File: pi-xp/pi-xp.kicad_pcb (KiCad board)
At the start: 2 copper layers, 30.5 x 65.4 mm, 25 parts

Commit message: pi_xp v1.1
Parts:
- F1: footprint Fuse_Holders_and_Fuses:BladeFuse-Mini_Keystone_3568 -> Fuse_Holders_and_Fuses:Fuse_TE5_Littlefuse-395Series
- OUT1, OUT2, OUT3: value CONN_01X03 -> CONN_01X02; footprint Pin_Headers:Pin_Header_Straight_1x03_Pitch2.54mm -> Pin_Headers:Pin_Header_Straight_1x02_Pitch2.54mm
- moved 5VIN1 52.2 mm to (94.6, 80.6), turned to 270 degrees
- moved F1 22.7 mm to (104.1, 132.1), turned to 180 degrees
- moved 12VOUT1 17.1 mm to (92.7, 109.2)
- moved 12VOUT2 16.5 mm to (92.7, 97.8)
- moved FAN1 16.2 mm to (92.7, 85.1), turned to 0 degrees
- moved OUT1 3.81 mm to (101.0, 125.7), turned to 180 degrees
- moved OUT2 3.81 mm to (104.8, 125.7), turned to 180 degrees
- moved OUT3 3.81 mm to (108.6, 125.7), turned to 180 degrees
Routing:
- net V12: track 0.00 -> 20.4 mm
- net PWM: track 31.1 -> 24.7 mm
- net OUTPUT1: track 17.7 -> 16.4 mm
- net OUTPUT2: track 12.8 -> 11.5 mm
- net GND: track 8.25 -> 7.62 mm
- net OUTPUT3: track 7.18 -> 6.66 mm
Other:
- board text added: "OyaMist PI_XP1.1"
- board text removed: "OyaMist PI_XP1.0"

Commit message: PI_XP1.2
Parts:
- OUT1, OUT2, OUT3: value CONN_01X02 -> CONN_01X03; footprint Pin_Headers:Pin_Header_Straight_1x02_Pitch2.54mm -> Pin_Headers:Pin_Header_Straight_1x03_Pitch2.54mm
- moved 12VIN1 1.27 mm to (92.7, 119.4)
- moved 12VOUT2 1.27 mm to (92.7, 99.1)
- moved OUT1 1.27 mm to (101.0, 127.0)
- moved OUT2 1.27 mm to (104.8, 127.0)
- moved OUT3 1.27 mm to (108.6, 127.0)
- moved FAN1 0.63 mm to (92.7, 85.7)
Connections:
- OUT1 pad 2: OUTPUT1 -> PI3V3
- OUT2 pad 2: OUTPUT2 -> PI3V3
- OUT3 pad 2: OUTPUT3 -> PI3V3
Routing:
- net OUTPUT1: track 16.4 -> 15.9 mm
- net OUTPUT2: track 11.5 -> 11.0 mm
- net OUTPUT3: track 6.66 -> 6.13 mm
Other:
- board text added: "OyaMist PI_XP1.2"
- board text removed: "OyaMist PI_XP1.1"

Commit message: v1.3
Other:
- board text added: "12V"
- board text added: "2"
- board text added: "3"
- board text added: "3V3"
- board text added: "IN"
- board text added: "OUT"
- board text added: "OyaMist PI_XP1.3"
- board text added: "PWM"
- board text added: "SCL"
- board text added: "SDA"
- board text added: "W1"
- board text added: "W1/1"
- board text removed: "1WIRE1"
- board text removed: "BLINK1"
- board text removed: "CLK"
- board text removed: "OyaMist PI_XP1.2"

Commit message: v1.3
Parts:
- moved BLINK1 1.77 mm to (109.2, 72.6)
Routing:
- net PI3V3_LED: track 5.23 -> 6.30 mm
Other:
- board text added: "39"
- board text added: "FUSE 5A/12V"
- board text added: "LED"
- board text added: "OyaMist Backplane"
- board text added: "PI-XP v1.3"
- board text removed: "FUSE 5A"
- board text removed: "OyaMist PI_XP1.3"

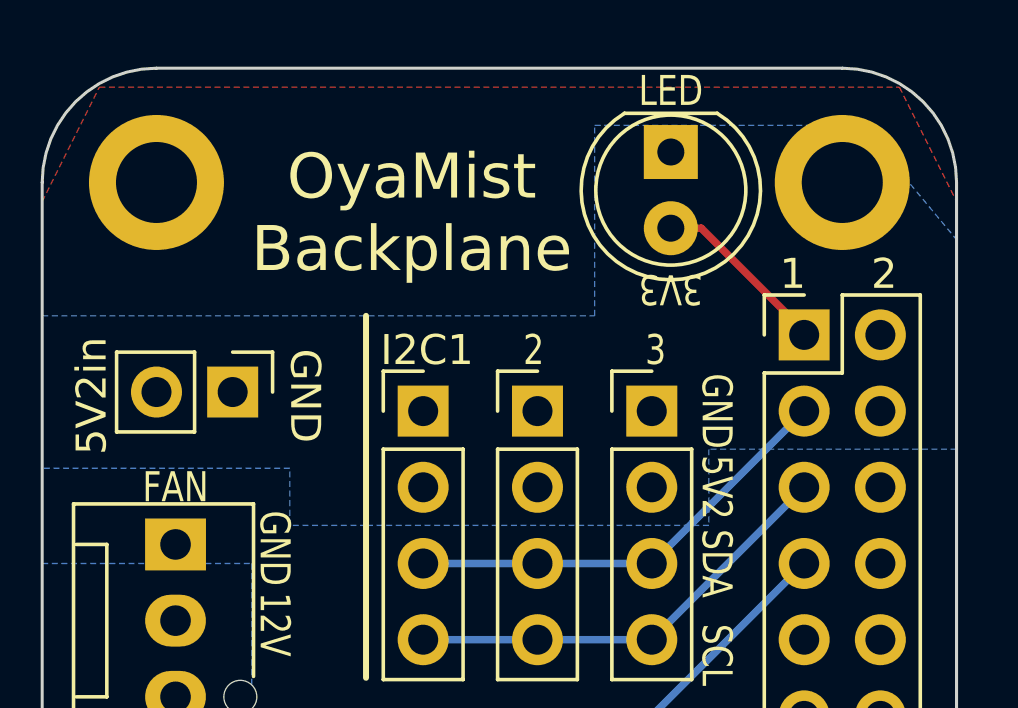
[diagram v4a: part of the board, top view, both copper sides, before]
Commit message: v1.4 I2C 3v3
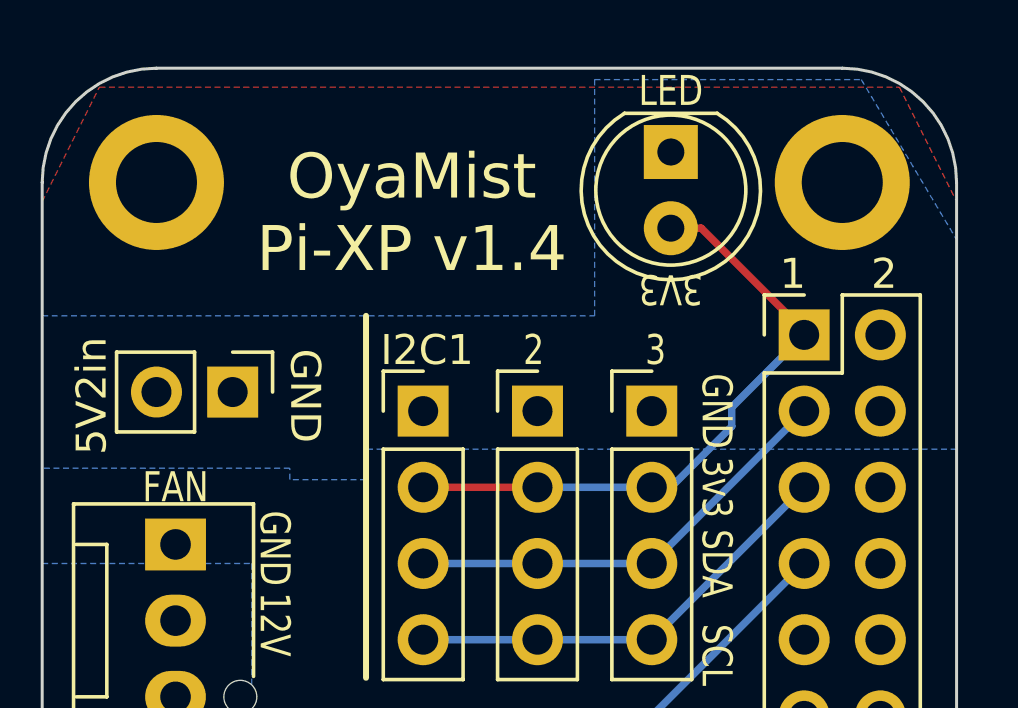
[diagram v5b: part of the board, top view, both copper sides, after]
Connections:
- I2C1 pad 2: 5V2 -> PI3V3_LED
- I2C2 pad 2: 5V2 -> PI3V3_LED
- I2C3 pad 2: 5V2 -> PI3V3_LED
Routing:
- net PI3V3_LED: track 6.30 -> 21.3 mm
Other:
- board text added: "Backplane"
- board text added: "OyaMist Pi-XP v1.4"
- board text removed: "5V2"
- board text removed: "OyaMist Backplane"
- board text removed: "PI-XP v1.3"
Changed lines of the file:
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@@
     (links 61)
     (no_connects 0)
-    (area 75.184 64.008 135.636 141.732)
+    (area 75.642857 64.135 135.635 141.765001)
     (thickness 1.6)
     (drawings 115)
-    (tracks 61)
+    (tracks 66)
     (zones 0)
     (modules 25)
@@
       (net 28 GND) (clearance -0.5))
     (pad 2 thru_hole oval (at 0 2.54) (size 1.7 1.7) (drill 1) (layers *.Cu *.Mask)
-      (net 30 5V2) (clearance -0.5))
+      (net 36 PI3V3_LED) (clearance -0.5))
     (pad 3 thru_hole oval (at 0 5.08) (size 1.7 1.7) (drill 1) (layers *.Cu *.Mask)
       (net 1 I2C_DAT))
@@
       (net 28 GND) (clearance -0.5))
     (pad 2 thru_hole oval (at 0 2.54) (size 1.7 1.7) (drill 1) (layers *.Cu *.Mask)
-      (net 30 5V2) (clearance -0.5))
+      (net 36 PI3V3_LED) (clearance -0.5))
     (pad 3 thru_hole oval (at 0 5.08) (size 1.7 1.7) (drill 1) (layers *.Cu *.Mask)
       (net 1 I2C_DAT))
@@
       (net 28 GND))
     (pad 2 thru_hole oval (at 0 2.54) (size 1.7 1.7) (drill 1) (layers *.Cu *.Mask)
-      (net 30 5V2) (clearance -1))
+      (net 36 PI3V3_LED) (clearance -1))
     (pad 3 thru_hole oval (at 0 5.08) (size 1.7 1.7) (drill 1) (layers *.Cu *.Mask)
       (net 1 I2C_DAT))
@@
     (effects (font (size 1 0.8) (thickness 0.15)) (justify mirror))
   )
-  (gr_text "PI-XP\nv1.3" (at 100.076 74.676) (layer B.SilkS)
+  (gr_text Backplane (at 100.838 71.882) (layer B.SilkS)
     (effects (font (size 1.5 1.5) (thickness 0.3)) (justify mirror))
   )
@@
     (effects (font (size 1 0.8) (thickness 0.15)) (justify mirror))
   )
-  (gr_text 5V2 (at 110.744 83.82 270) (layer B.SilkS)
+  (gr_text "3v3\n" (at 110.744 83.82 270) (layer B.SilkS)
     (effects (font (size 1 0.8) (thickness 0.15)) (justify mirror))
   )
@@
     (effects (font (size 1 0.8) (thickness 0.15)))
   )
-  (gr_text 5V2 (at 110.744 83.82 270) (layer F.SilkS)
+  (gr_text "3v3\n" (at 110.744 83.82 270) (layer F.SilkS)
     (effects (font (size 1 0.8) (thickness 0.15)))
   )
@@
     (effects (font (size 1 0.8) (thickness 0.15)))
   )
-  (gr_text "OyaMist\nBackplane\n" (at 100.584 74.676) (layer F.SilkS)
+  (gr_text "OyaMist\nPi-XP v1.4\n" (at 100.584 74.676) (layer F.SilkS)
     (effects (font (size 1.5 1.5) (thickness 0.3)))
   )
@@
   (segment (start 108.585 114.3) (end 104.775 114.3) (width 1) (layer B.Cu) (net 28) (status 80030))
   (segment (start 104.775 114.3) (end 100.965 114.3) (width 1) (layer B.Cu) (net 28) (status 80030))
-  (segment (start 113.665 78.74) (end 113.792 78.74) (width 0.25) (layer F.Cu) (net 36) (status 80000))
-  (segment (start 113.792 78.74) (end 110.236 75.184) (width 0.25) (layer F.Cu) (net 36) (status 80000))
-  (segment (start 110.236 75.184) (end 109.22 75.184) (width 0.25) (layer F.Cu) (net 36) (status 80000))
-  (segment (start 113.665 78.74) (end 113.792 78.74) (width 0.25) (layer F.Cu) (net 36) (status 80000))
+  (segment (start 108.585 83.82) (end 109.22 83.82) (width 0.25) (layer B.Cu) (net 36) (status 30))
+  (segment (start 109.22 83.82) (end 111.252 81.788) (width 0.25) (layer B.Cu) (net 36) (status 10))
+  (segment (start 111.252 81.153) (end 113.665 78.74) (width 0.25) (layer B.Cu) (net 36) (status 20))
+  (segment (start 111.252 81.788) (end 111.252 81.153) (width 0.25) (layer B.Cu) (net 36))
+  (segment (start 104.775 83.82) (end 100.965 83.82) (width 0.25) (layer F.Cu) (net 36) (status 80030))
+  (segment (start 108.585 83.82) (end 104.775 83.82) (width 0.25) (layer B.Cu) (net 36) (status 80030))
+  (segment (start 113.665 78.74) (end 113.792 78.74) (width 0.25) (layer F.Cu) (net 36) (status 80030))
+  (segment (start 113.792 78.74) (end 110.236 75.184) (width 0.25) (layer F.Cu) (net 36) (status 80010))
+  (segment (start 110.236 75.184) (end 109.22 75.184) (width 0.25) (layer F.Cu) (net 36) (status 80020))
   (zone (net 3) (net_name PI3V3) (layer B.Cu) (hatch edge 0.508)
     (connect_pads (clearance 0.508))
@@
     (polygon
       (pts
-        (xy 118.745 75.565) (xy 118.745 82.55) (xy 110.49 82.55) (xy 110.49 85.09) (xy 99.06 85.09)
-        (xy 99.06 85.09) (xy 96.52 85.09) (xy 96.52 83.185) (xy 88.265 83.185) (xy 88.265 78.105)
-        (xy 106.68 78.105) (xy 106.68 71.755) (xy 115.57 71.755) (xy 118.745 75.565)
+        (xy 118.745 75.565) (xy 118.745 82.55) (xy 110.49 82.55) (xy 110.49 82.55) (xy 99.06 82.55)
+        (xy 99.06 83.566) (xy 96.52 83.566) (xy 96.52 83.185) (xy 88.265 83.185) (xy 88.265 78.105)
+        (xy 106.68 78.105) (xy 106.68 70.231) (xy 115.57 70.231) (xy 118.745 75.565)
       )
     )

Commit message: Dowel
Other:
- board text added: "OyaMist Pi-XPv1.4"
- board text removed: "OyaMist Pi-XP v1.4"
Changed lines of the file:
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@@
     (effects (font (size 1 0.8) (thickness 0.15)))
   )
-  (gr_text "OyaMist\nPi-XP v1.4\n" (at 100.584 74.676) (layer F.SilkS)
+  (gr_text "OyaMist\nPi-XPv1.4\n" (at 100.076 75.184) (layer F.SilkS)
     (effects (font (size 1.5 1.5) (thickness 0.3)))
   )
